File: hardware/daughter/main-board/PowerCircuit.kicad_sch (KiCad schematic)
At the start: 32 parts, among them J9 Barrel_Jack, U31 XTPS55285VALR, U32 TPS54202DDC, U33 LM2776

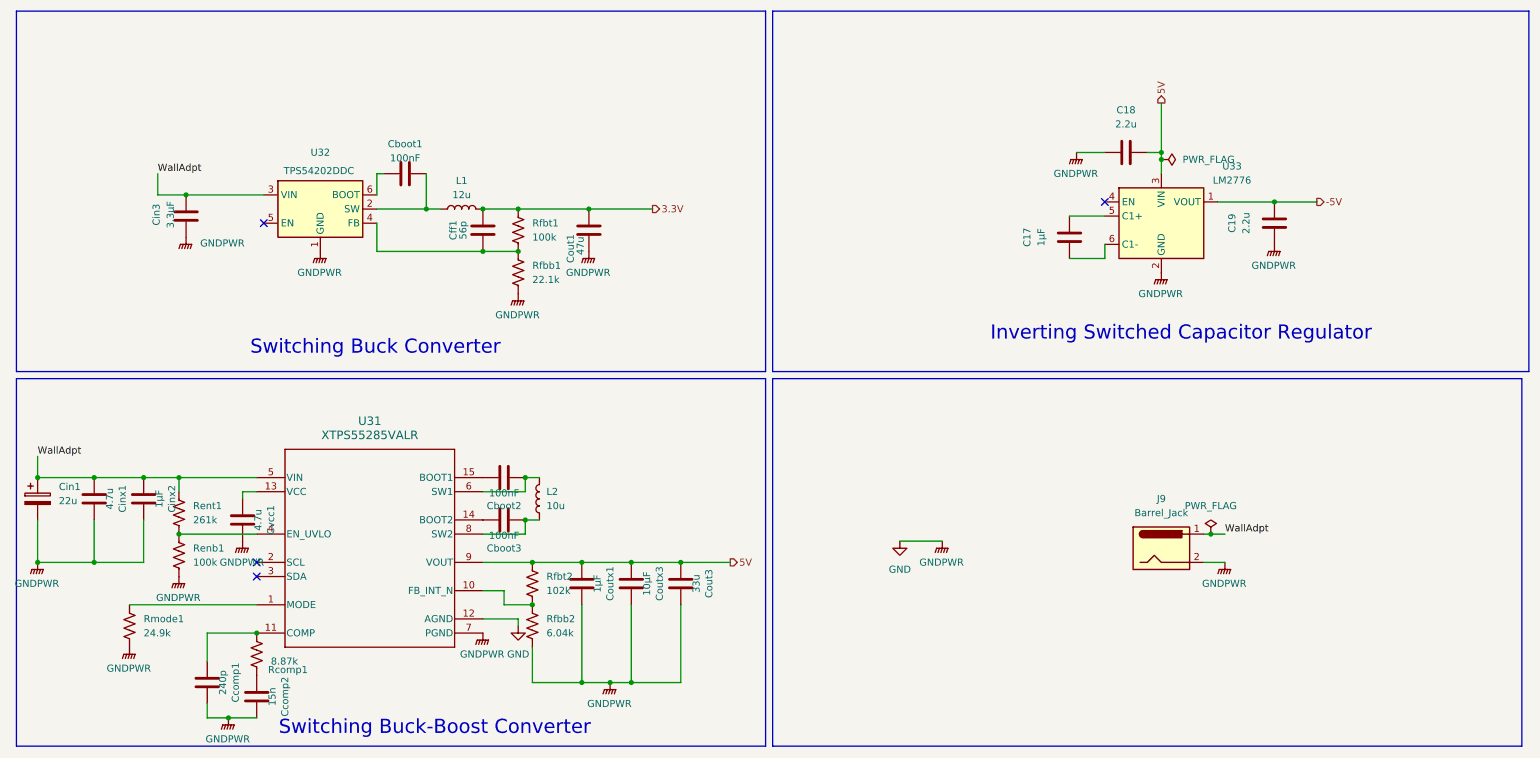
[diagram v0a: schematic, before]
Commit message: formatted heirarchical
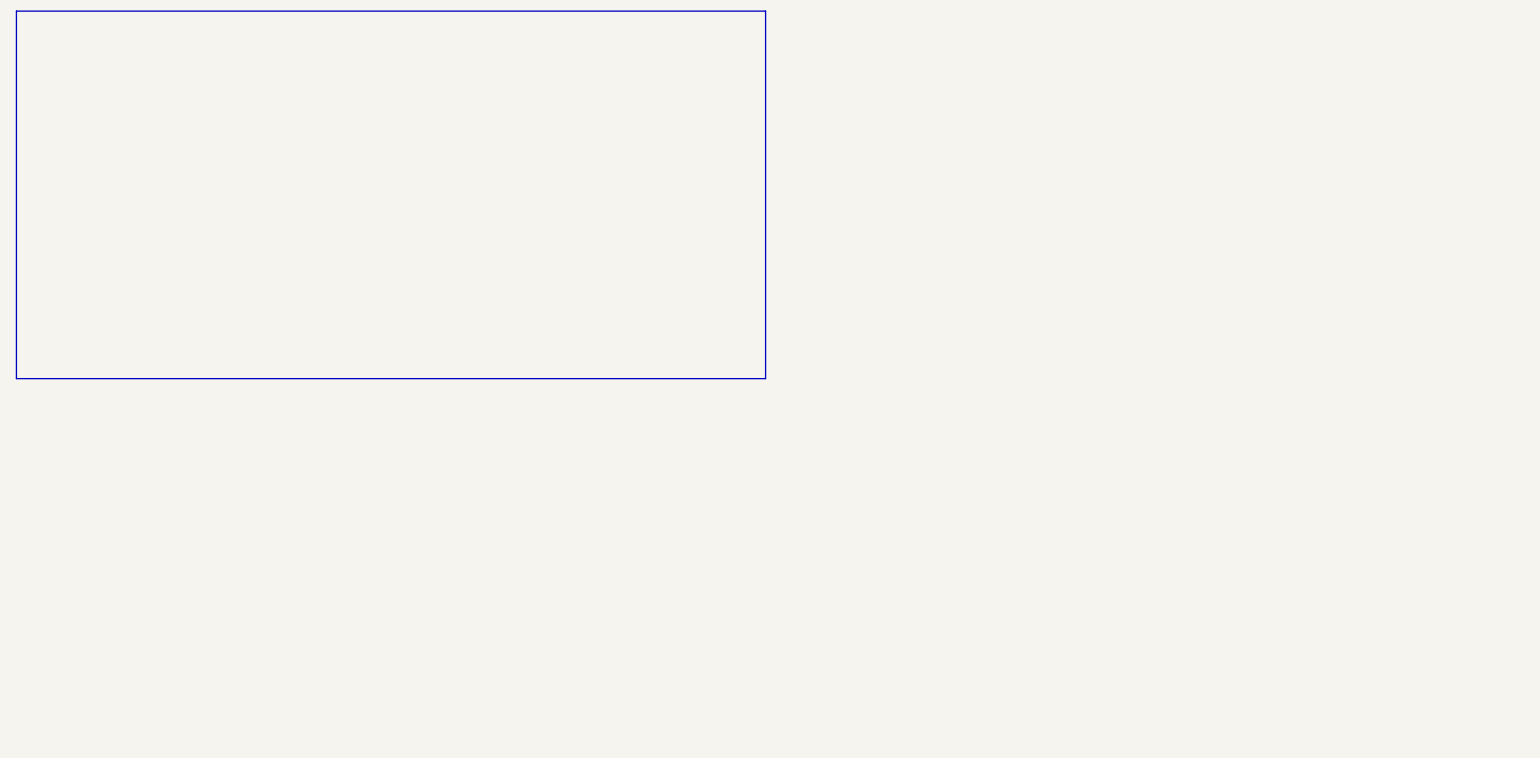
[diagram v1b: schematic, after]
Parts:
- removed C17: 1µF, Capacitor_SMD:C_0603_1608Metric_Pad1.08x0.95mm_HandSolder, symbol Device:C
- removed C18, C19: 2.2u, Capacitor_SMD:C_0603_1608Metric_Pad1.08x0.95mm_HandSolder, symbol Device:C
- removed Cboot1: 100nF, Capacitor_SMD:C_0805_2012Metric_Pad1.18x1.45mm_HandSolder, symbol Device:C
- removed Cboot2, Cboot3: 100nF, Capacitor_SMD:C_0402_1005Metric_Pad0.74x0.62mm_HandSolder, symbol Device:C
- removed Ccomp1: 240p, Capacitor_SMD:C_0402_1005Metric_Pad0.74x0.62mm_HandSolder, symbol Device:C
- removed Ccomp2: 15n, Capacitor_SMD:C_0402_1005Metric_Pad0.74x0.62mm_HandSolder, symbol Device:C
- removed Cff1: 56p, Capacitor_SMD:C_0201_0603Metric_Pad0.64x0.40mm_HandSolder, symbol Device:C
- removed Cin1: 22u, SeniorDesignFP:CAP_EEFK_C_PAN, symbol Device:C_Polarized
- removed Cin3: 3.3µF, Capacitor_SMD:C_1210_3225Metric_Pad1.33x2.70mm_HandSolder, symbol Device:C
- removed Cinx1: 4.7u, Capacitor_SMD:C_1210_3225Metric_Pad1.33x2.70mm_HandSolder, symbol Device:C
- removed Cinx2: 1µF, Capacitor_SMD:C_0402_1005Metric_Pad0.74x0.62mm_HandSolder, symbol Device:C
- removed Cout1: 47u, Capacitor_SMD:C_0805_2012Metric_Pad1.18x1.45mm_HandSolder, symbol Device:C
- removed Cout3: 33u, Capacitor_Tantalum_SMD:CP_EIA-3528-21_Kemet-B_HandSolder, symbol Device:C
- removed Coutx1: 1µF, Capacitor_SMD:C_0201_0603Metric_Pad0.64x0.40mm_HandSolder, symbol Device:C
- removed Coutx3: 10µF, Capacitor_SMD:C_1210_3225Metric_Pad1.33x2.70mm_HandSolder, symbol Device:C
- removed Cvcc1: 4.7u, Capacitor_SMD:C_0201_0603Metric_Pad0.64x0.40mm_HandSolder, symbol Device:C
- removed J9: Barrel_Jack, Connector_BarrelJack:BarrelJack_CUI_PJ-063AH_Horizontal, symbol Connector:Barrel_Jack
- removed L1: 12u, SeniorDesignFP:IND_4532-WE-PD2_WRE-L, symbol Device:L
- removed L2: 10u, Inductor_SMD:L_Bourns_SRN6045TA, symbol Device:L
- removed Rcomp1: 8.87k, Resistor_SMD:R_0402_1005Metric_Pad0.72x0.64mm_HandSolder, symbol Device:R_US
- removed Renb1, Rfbt1: 100k, Resistor_SMD:R_0402_1005Metric_Pad0.72x0.64mm_HandSolder, symbol Device:R_US
- removed Rent1: 261k, Resistor_SMD:R_0402_1005Metric_Pad0.72x0.64mm_HandSolder, symbol Device:R_US
- removed Rfbb1: 22.1k, Resistor_SMD:R_0402_1005Metric_Pad0.72x0.64mm_HandSolder, symbol Device:R_US
- removed Rfbb2: 6.04k, Resistor_SMD:R_0402_1005Metric_Pad0.72x0.64mm_HandSolder, symbol Device:R_US
- removed Rfbt2: 102k, Resistor_SMD:R_0402_1005Metric_Pad0.72x0.64mm_HandSolder, symbol Device:R_US
- removed Rmode1: 24.9k, Resistor_SMD:R_0402_1005Metric_Pad0.72x0.64mm_HandSolder, symbol Device:R_US
- removed U31: XTPS55285VALR, SeniorDesignFP:TPS55285, symbol SeniorDesign:XTPS55285VALR
- removed U32: TPS54202DDC, Package_TO_SOT_SMD:SOT-23-6, symbol Regulator_Switching:TPS54202DDC
- removed U33: LM2776, Package_TO_SOT_SMD:SOT-23-6, symbol Regulator_SwitchedCapacitor:LM2776
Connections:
- no-connect marks 4 -> 0
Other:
- note removed: "Inverting Switched Capacitor Regulator"
- note removed: "Switching Buck Converter"
- note removed: "Switching Buck-Boost Converter"
